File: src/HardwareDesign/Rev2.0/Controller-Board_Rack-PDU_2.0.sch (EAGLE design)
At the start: 98 parts, among them IC1 W5500, IC2 RP2040, IC3 MCP6001R, IC4 W25Q128JVPIQ, IC5 MIC5504-3.3YM5-TR, IC6 CAT24C512HU5IGT3, X1 XC53M4-25.000-F18NJDTL, X2 K5A1200015304P

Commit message: source code - pre version. Never RP2040 or any RP series ever. Copiling to this is nightmare
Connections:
- net !INT renamed !W5500_INT
- net !RST renamed !W5500_RST
- net !SPI0_CS renamed !W5500_CS
- net SPI0_MISO renamed W5500_MISO
- net SPI0_MOSI renamed W5500_MOSI
- net SPI0_SCK renamed W5500_SCK
- net V_USB renamed ADC_V_USB
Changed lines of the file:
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@@
 </segment>
 </net>
-<net name="SPI0_SCK" class="0">
+<net name="W5500_SCK" class="0">
 <segment>
 <pinref part="IC2" gate="G$1" pin="GPIO18"/>
@@
 </segment>
 </net>
-<net name="SPI0_MISO" class="0">
+<net name="W5500_MISO" class="0">
 <segment>
 <pinref part="IC2" gate="G$1" pin="GPIO16"/>
@@
 </segment>
 </net>
-<net name="SPI0_MOSI" class="0">
+<net name="W5500_MOSI" class="0">
 <segment>
 <pinref part="IC2" gate="G$1" pin="GPIO19"/>
@@
 </segment>
 </net>
-<net name="!INT" class="0">
+<net name="!W5500_INT" class="0">
 <segment>
 <pinref part="IC2" gate="G$1" pin="GPIO21"/>
@@
 </segment>
 </net>
-<net name="!RST" class="0">
+<net name="!W5500_RST" class="0">
 <segment>
 <pinref part="IC2" gate="G$1" pin="GPIO20"/>
@@
 </segment>
 </net>
-<net name="!SPI0_CS" class="0">
+<net name="!W5500_CS" class="0">
 <segment>
 <pinref part="IC2" gate="G$1" pin="GPIO17"/>
@@
 </segment>
 </net>
-<net name="V_USB" class="0">
+<net name="ADC_V_USB" class="0">
 <segment>
 <pinref part="R25" gate="G$1" pin="2"/>
@@
 </segment>
 </net>
-<net name="!SPI0_CS" class="0">
+<net name="!W5500_CS" class="0">
 <segment>
 <pinref part="IC1" gate="G$1" pin="!SCSN"/>
@@
 </segment>
 </net>
-<net name="SPI0_SCK" class="0">
+<net name="W5500_SCK" class="0">
 <segment>
 <pinref part="IC1" gate="G$1" pin="SCLK"/>
@@
 </segment>
 </net>
-<net name="SPI0_MISO" class="0">
+<net name="W5500_MISO" class="0">
 <segment>
 <pinref part="IC1" gate="G$1" pin="MISO"/>
@@
 </segment>
 </net>
-<net name="SPI0_MOSI" class="0">
+<net name="W5500_MOSI" class="0">
 <segment>
 <pinref part="IC1" gate="G$1" pin="MOSI"/>
@@
 </segment>
 </net>
-<net name="!INT" class="0">
+<net name="!W5500_INT" class="0">
 <segment>
 <pinref part="IC1" gate="G$1" pin="!INTN"/>
@@
 </segment>
 </net>
-<net name="!RST" class="0">
+<net name="!W5500_RST" class="0">
 <segment>
 <pinref part="IC1" gate="G$1" pin="!RSTN"/>

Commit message: correct findings
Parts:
- added R12, R29: 10K, ds_passive:R0402
- R27: value 4.7K -> NC
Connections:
- net +3V3: now also R12.2, R29.2
- net MCP_DSP_RST: now also R12.1
- net MCP_REL_RST: now also R29.1
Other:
- moved on the sheet: DISPBOARD

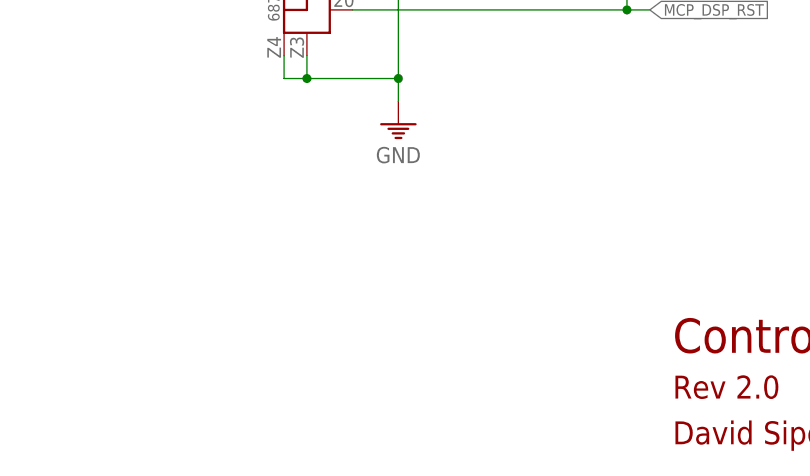
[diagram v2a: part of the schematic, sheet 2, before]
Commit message: I2C, SPI-DMA, EEPROM driver ready
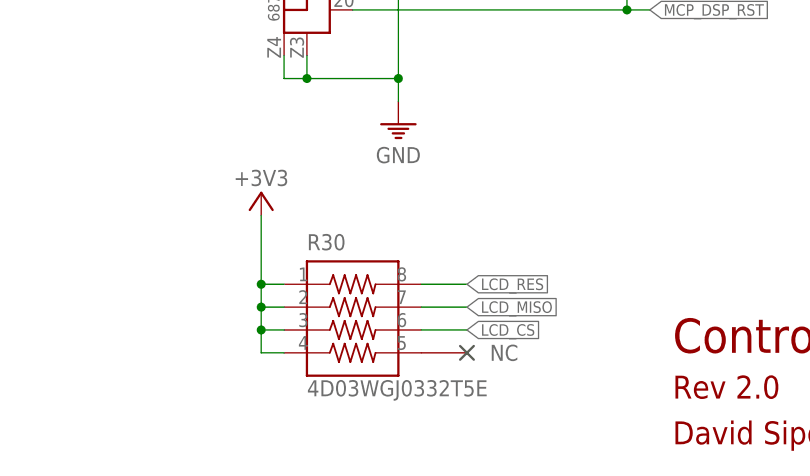
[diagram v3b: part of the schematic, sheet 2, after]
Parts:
- added R30: 4D03WGJ0332T5E, Resistor Array:742C083103JP
- BOOT, RESET: value 430182043816 -> RS032G05A3SM-SPST-MOMENTARY-SWSMD-1101NE; device Wurth_Switch_WS-TASV:430182043816 -> BeagleBone_Blue_R3:RS032G05A3SM-SPST-MOMENTARY-SWSMD-1101NE
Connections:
- net +3V3: now also R30.1, R30.2, R30.3, R30.4
- net GND: now also BOOT.2; no longer BOOT.3, BOOT.4, RESET.2
- net LCD_CS: now also R30.6
- net LCD_MISO: now also R30.7
- net LCD_RES: now also R30.8
- net N$17: now also RESET.2; no longer RESET.3, RESET.4
- net USB_BOOT: no longer BOOT.2
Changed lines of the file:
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@@
 <?xml version="1.0" encoding="utf-8"?>
 <!DOCTYPE eagle SYSTEM "eagle.dtd">
-<eagle version="9.6.2">
+<eagle version="9.2.1">
 <drawing>
 <settings>
@@
 <part name="NC20" library="ds_passive" deviceset="NC" device=""/>
 <part name="DISPBOARD" library="Wurth_Connectors_WR-FPC" library_urn="urn:adsk.eagle:library:15778639" deviceset="6873XX124422_687320124422" device="" package3d_urn="urn:adsk.eagle:package:15743882/4" value="687320124422"/>
-<part name="BOOT" library="Wurth_Switch_WS-TASV" library_urn="urn:adsk.eagle:library:18304196" deviceset="430182043816" device="" package3d_urn="urn:adsk.eagle:package:18304300/2" value="430182043816"/>
-<part name="RESET" library="Wurth_Switch_WS-TASV" library_urn="urn:adsk.eagle:library:18304196" deviceset="430182043816" device="" package3d_urn="urn:adsk.eagle:package:18304300/2" value="430182043816"/>
 <part name="R12" library="ds_passive" deviceset="R" device="0402" package3d_urn="urn:adsk.eagle:package:46683744/2" value="10K"/>
 <part name="+3V17" library="ds_passive" deviceset="+3V3" device=""/>
 <part name="R29" library="ds_passive" deviceset="R" device="0402" package3d_urn="urn:adsk.eagle:package:46683744/2" value="10K"/>
 <part name="+3V18" library="ds_passive" deviceset="+3V3" device=""/>
+<part name="BOOT" library="BeagleBone_Blue_R3" library_urn="urn:adsk.eagle:library:5828899" deviceset="RS032G05A3SM-SPST-MOMENTARY-SW" device="SMD-1101NE" package3d_urn="urn:adsk.eagle:package:5829833/3"/>
+<part name="RESET" library="BeagleBone_Blue_R3" library_urn="urn:adsk.eagle:library:5828899" deviceset="RS032G05A3SM-SPST-MOMENTARY-SW" device="SMD-1101NE" package3d_urn="urn:adsk.eagle:package:5829833/3"/>
+<part name="R30" library="Resistor Array" library_urn="urn:adsk.eagle:library:16491332" deviceset="742C083103JP" device="" package3d_urn="urn:adsk.eagle:package:16445849/4" value="4D03WGJ0332T5E"/>
+<part name="NC3" library="ds_passive" deviceset="NC" device=""/>
+<part name="+3V21" library="ds_passive" deviceset="+3V3" device=""/>
 </parts>
 <sheets>
@@
 <instance part="NC21" gate="G$1" x="187.96" y="137.16" smashed="yes"/>
 <instance part="NC22" gate="G$1" x="187.96" y="134.62" smashed="yes"/>
-<instance part="BOOT" gate="G$1" x="83.82" y="127" smashed="yes">
-<attribute name="NAME" x="83.82" y="132.842" size="1.778" layer="95" align="bottom-center"/>
-<attribute name="VALUE" x="81.28" y="121.92" size="1.778" layer="96" align="bottom-center"/>
-</instance>
-<instance part="RESET" gate="G$1" x="109.22" y="215.9" smashed="yes">
-<attribute name="NAME" x="109.22" y="221.742" size="1.778" layer="95" align="bottom-center"/>
-<attribute name="VALUE" x="109.22" y="210.82" size="1.778" layer="96" align="bottom-center"/>
+<instance part="BOOT" gate="G$1" x="83.82" y="124.46" smashed="yes">
+<attribute name="NAME" x="81.28" y="127" size="1.778" layer="95"/>
+<attribute name="VALUE" x="81.28" y="121.92" size="1.778" layer="96"/>
+</instance>
+<instance part="RESET" gate="G$1" x="109.22" y="213.36" smashed="yes">
+<attribute name="NAME" x="106.68" y="215.9" size="1.778" layer="95"/>
+<attribute name="VALUE" x="106.68" y="210.82" size="1.778" layer="96"/>
 </instance>
 </instances>
@@
 <wire x1="91.44" y1="124.46" x2="91.44" y2="121.92" width="0.1524" layer="91"/>
 <pinref part="GND37" gate="1" pin="GND"/>
-<pinref part="BOOT" gate="G$1" pin="4"/>
-<pinref part="BOOT" gate="G$1" pin="3"/>
-<wire x1="88.9" y1="132.08" x2="91.44" y2="132.08" width="0.1524" layer="91"/>
-<wire x1="91.44" y1="132.08" x2="91.44" y2="124.46" width="0.1524" layer="91"/>
-<junction x="91.44" y="124.46"/>
+<pinref part="BOOT" gate="G$1" pin="2"/>
 </segment>
 <segment>
@@
 <wire x1="99.06" y1="213.36" x2="99.06" y2="210.82" width="0.1524" layer="91"/>
 <pinref part="GND50" gate="1" pin="GND"/>
-<pinref part="RESET" gate="G$1" pin="2"/>
-<pinref part="RESET" gate="G$1" pin="1"/>
 <wire x1="104.14" y1="220.98" x2="99.06" y2="220.98" width="0.1524" layer="91"/>
 <wire x1="99.06" y1="220.98" x2="99.06" y2="213.36" width="0.1524" layer="91"/>
 <junction x="99.06" y="213.36"/>
+<pinref part="RESET" gate="G$1" pin="1"/>
 </segment>
 </net>
@@
 </segment>
 <segment>
-<wire x1="78.74" y1="124.46" x2="73.66" y2="124.46" width="0.1524" layer="91"/>
 <label x="68.58" y="124.46" size="1.27" layer="95" rot="R180" xref="yes"/>
-<pinref part="BOOT" gate="G$1" pin="2"/>
+<wire x1="78.74" y1="124.46" x2="68.58" y2="124.46" width="0.1524" layer="91"/>
 <pinref part="BOOT" gate="G$1" pin="1"/>
-<wire x1="73.66" y1="124.46" x2="68.58" y2="124.46" width="0.1524" layer="91"/>
-<wire x1="78.74" y1="132.08" x2="73.66" y2="132.08" width="0.1524" layer="91"/>
-<wire x1="73.66" y1="132.08" x2="73.66" y2="124.46" width="0.1524" layer="91"/>
-<junction x="73.66" y="124.46"/>
 </segment>
 </net>
@@
 <junction x="121.92" y="213.36"/>
 <pinref part="R50" gate="G$1" pin="2"/>
-<pinref part="RESET" gate="G$1" pin="4"/>
-<pinref part="RESET" gate="G$1" pin="3"/>
 <wire x1="114.3" y1="220.98" x2="116.84" y2="220.98" width="0.1524" layer="91"/>
 <wire x1="116.84" y1="220.98" x2="116.84" y2="213.36" width="0.1524" layer="91"/>
 <junction x="116.84" y="213.36"/>
+<pinref part="RESET" gate="G$1" pin="2"/>
 </segment>
 </net>
@@
 <attribute name="VALUE" x="358.14" y="88.9" size="1.778" layer="96" rot="MR0" align="top-center"/>
 </instance>
+<instance part="R30" gate="G$1" x="254" y="22.86" smashed="yes">
+<attribute name="NAME" x="248.92" y="29.1846" size="1.778" layer="95"/>
+<attribute name="VALUE" x="248.92" y="12.954" size="1.778" layer="96"/>
+</instance>
+<instance part="NC3" gate="G$1" x="266.7" y="17.78" smashed="yes" rot="MR180"/>
+<instance part="+3V21" gate="G$1" x="243.84" y="35.56" smashed="yes" rot="MR0">
+<attribute name="VALUE" x="243.84" y="38.1" size="1.778" layer="96" rot="MR0" align="top-center"/>
+</instance>
 </instances>
 <busses>
@@
 <pinref part="+3V18" gate="G$1" pin="+3V3"/>
 <wire x1="358.14" y1="83.82" x2="358.14" y2="81.28" width="0.1524" layer="91"/>
+</segment>
+<segment>
+<pinref part="R30" gate="G$1" pin="1"/>
+<wire x1="246.38" y1="25.4" x2="243.84" y2="25.4" width="0.1524" layer="91"/>
+<wire x1="243.84" y1="25.4" x2="243.84" y2="33.02" width="0.1524" layer="91"/>
+<pinref part="R30" gate="G$1" pin="2"/>
+<wire x1="246.38" y1="22.86" x2="243.84" y2="22.86" width="0.1524" layer="91"/>
+<wire x1="243.84" y1="22.86" x2="243.84" y2="25.4" width="0.1524" layer="91"/>
+<junction x="243.84" y="25.4"/>
+<pinref part="R30" gate="G$1" pin="3"/>
+<wire x1="246.38" y1="20.32" x2="243.84" y2="20.32" width="0.1524" layer="91"/>
+<wire x1="243.84" y1="20.32" x2="243.84" y2="22.86" width="0.1524" layer="91"/>
+<junction x="243.84" y="22.86"/>
+<pinref part="R30" gate="G$1" pin="4"/>
+<wire x1="246.38" y1="17.78" x2="243.84" y2="17.78" width="0.1524" layer="91"/>
+<wire x1="243.84" y1="17.78" x2="243.84" y2="20.32" width="0.1524" layer="91"/>
+<junction x="243.84" y="20.32"/>
+<pinref part="+3V21" gate="G$1" pin="+3V3"/>
 </segment>
 </net>
@@
 <pinref part="DISPBOARD" gate="G$1" pin="19"/>
 </segment>
+<segment>
+<pinref part="R30" gate="G$1" pin="6"/>
+<wire x1="261.62" y1="20.32" x2="266.7" y2="20.32" width="0.1524" layer="91"/>
+<label x="266.7" y="20.32" size="1.27" layer="95" xref="yes"/>
+</segment>
 </net>
 <net name="LCD_MOSI" class="0">
@@
 <label x="264.16" y="71.12" size="1.27" layer="95" xref="yes"/>
 <pinref part="DISPBOARD" gate="G$1" pin="14"/>
+</segment>
+<segment>
+<pinref part="R30" gate="G$1" pin="8"/>
+<wire x1="261.62" y1="25.4" x2="266.7" y2="25.4" width="0.1524" layer="91"/>
+<label x="266.7" y="25.4" size="1.27" layer="95" xref="yes"/>
 </segment>
 </net>
@@
 <pinref part="DISPBOARD" gate="G$1" pin="15"/>
 </segment>
-</net>
+<segment>
+<pinref part="R30" gate="G$1" pin="7"/>
+<wire x1="261.62" y1="22.86" x2="266.7" y2="22.86" width="0.1524" layer="91"/>
+<label x="266.7" y="22.86" size="1.27" layer="95" xref="yes"/>
+</segment>
+</net>
